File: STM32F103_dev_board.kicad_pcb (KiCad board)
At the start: 4 copper layers, 39.4 x 83.8 mm, 37 parts, among them IC1 TLV70233DBVR, IC2 FT232RNL-REEL, J1 Conn_ARM_JTAG_SWD_20, J2 Conn_01x20_Pin, J3 Conn_01x20_Pin, J4 Conn_02x03_Odd_Even, J6 USB4800-03-A, U1 STM32F103RBTx, Y1 8MHz, Y2 Crystal_GND23

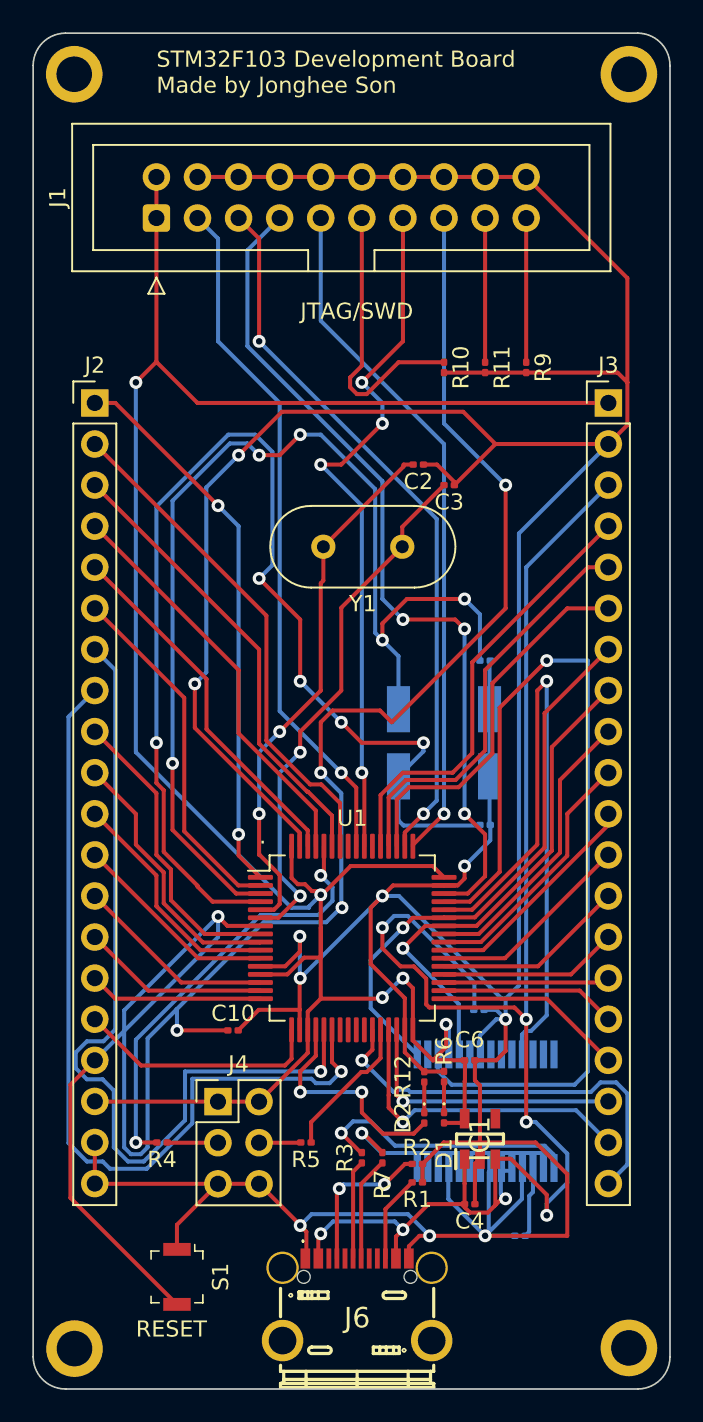
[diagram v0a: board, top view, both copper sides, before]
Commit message: Changed 0603 footprints to hand solderable ones
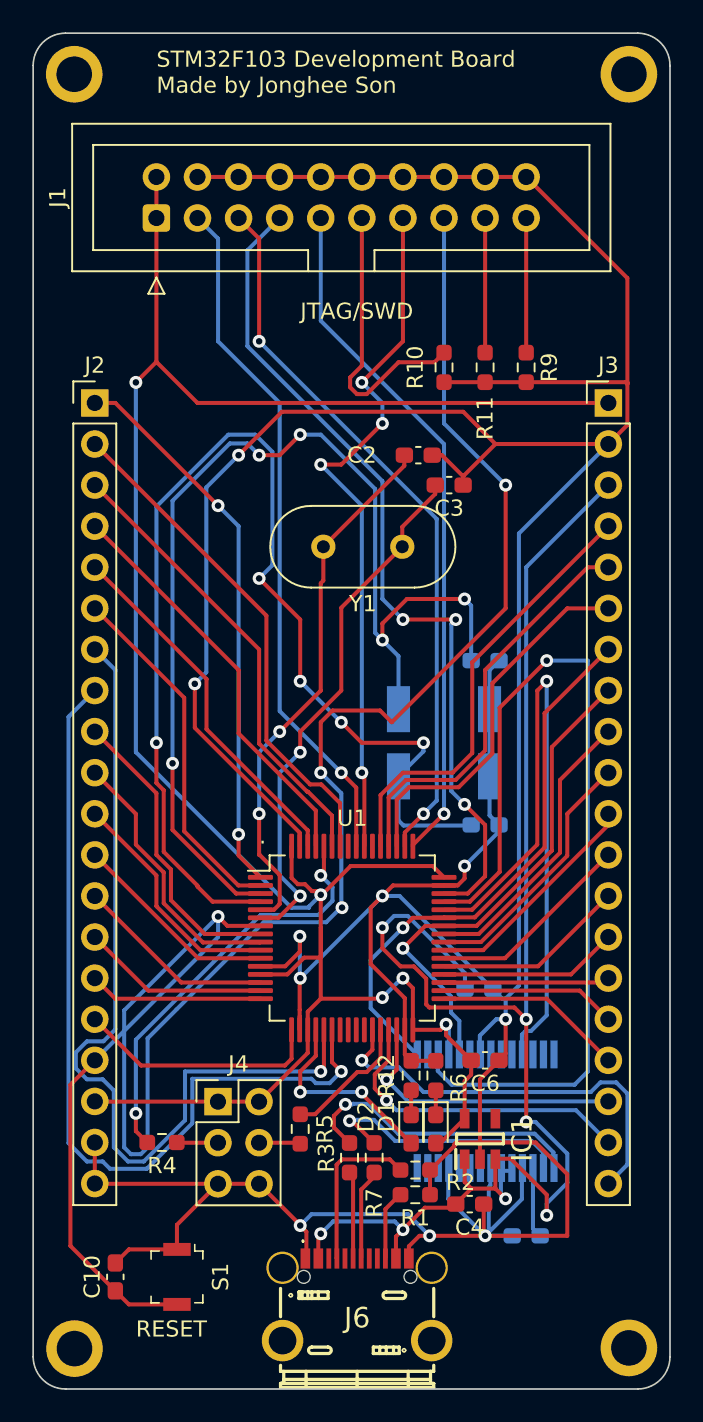
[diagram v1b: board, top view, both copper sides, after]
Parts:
- C1, C10, C11, C12, C2, C3, C4, C5, C6: footprint Capacitor_SMD:C_0201_0603Metric -> Capacitor_SMD:C_0603_1608Metric_Pad1.08x0.95mm_HandSolder
- D1, D2: footprint LED_SMD:LED_0201_0603Metric -> LED_SMD:LED_0603_1608Metric_Pad1.05x0.95mm_HandSolder
- R1, R10, R11, R12, R2, R3, R4, R5, R6, R7, R9: footprint Resistor_SMD:R_0201_0603Metric -> Resistor_SMD:R_0603_1608Metric_Pad0.98x0.95mm_HandSolder
- moved C10 16.9 mm to (130.8, 134.6), turned to 90 degrees
- moved C1 1.27 mm to (153.3, 116.8)
- moved D2 1.06 mm to (149.1, 125.5)
- moved C6 0.95 mm to (153.7, 121.2)
- moved R5 0.91 mm to (142.2, 125.5), turned to -90 degrees
- moved D1 0.86 mm to (150.6, 125.5)
- moved R12 0.81 mm to (149.1, 122.2)
- moved R1 0.77 mm to (149.4, 129.5)
- moved R3 0.76 mm to (145.3, 127.3)
- moved C2 0.58 mm to (149.5, 83.8)
- moved R6 0.51 mm to (150.6, 122.2)
- moved R7 0.51 mm to (146.8, 127.3)
- moved R2 0.40 mm to (149.4, 128.0)
- moved C5 0.38 mm to (156.2, 132.1)
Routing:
- net /5V: track 101.8 -> 98.7 mm
- net /GND: track 307.3 -> 304.3 mm
- net /RESET: track 278.4 -> 275.7 mm, vias 10 -> 9
- net /PA4: track 14.0 -> 12.5 mm
- net /USBDM: track 14.5 -> 15.9 mm
- net /USBDP: track 17.0 -> 18.3 mm
- net Net-(J6-CC2): track 5.39 -> 4.35 mm
- net /BOOT0: track 27.1 -> 26.1 mm
- net Net-(J6-DN1): track 6.50 -> 5.65 mm
- net /BOOT1: track 8.94 -> 8.15 mm
- net Net-(J6-DP1): track 6.13 -> 5.41 mm
- net Net-(J6-CC1): track 9.52 -> 10.2 mm, vias 2 -> 0
- net Net-(J4-Pin_3): track 3.15 -> 2.55 mm
- net Net-(J1-DBGRQ/NC): track 8.92 -> 8.32 mm
- net Net-(J1-DBGACK/NC): track 8.92 -> 8.32 mm
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
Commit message: Fixed some labels and updated production files
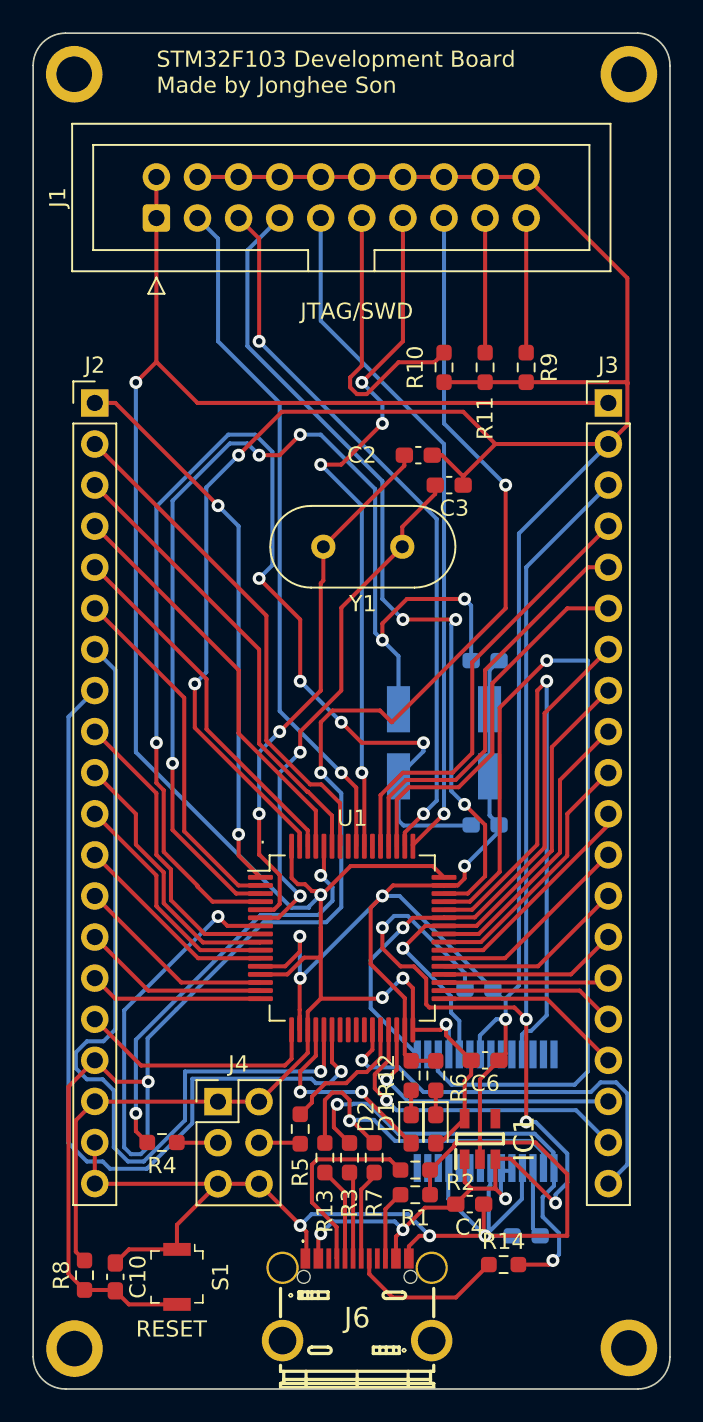
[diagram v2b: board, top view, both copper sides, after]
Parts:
- added R13: 20, Resistor_SMD:R_0603_1608Metric_Pad0.98x0.95mm_HandSolder, F.Cu at (143.8, 127.3)
- added R14: 20, Resistor_SMD:R_0603_1608Metric_Pad0.98x0.95mm_HandSolder, F.Cu at (154.8, 133.9)
- added R8: 0, Resistor_SMD:R_0603_1608Metric_Pad0.98x0.95mm_HandSolder, F.Cu at (128.9, 134.5)
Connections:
- net /5V renamed 5V
- net /GND renamed GND
- net /PA10/USART1_RX renamed PA10/USART1_RX
- net /PA9/USART1_TX renamed PA9/USART1_TX
- net /USBDM renamed USBDM
- net /USBDP renamed USBDP
- net /VBAT renamed VBAT
- C10 pad 1: /RESET -> RESET
- C6 pad 2: /RESET -> VCC3V3
- D1 pad 2: /RESET -> VCC3V3
- IC1 pad 5: /RESET -> VCC3V3
- IC2 pad 4: /RESET -> VCC3V3
- J1 pad 1: /RESET -> VCC3V3
- J1 pad 15: /RESET -> RESET
- J1 pad 2: /RESET -> VCC3V3
- J2 pad 17: /RESET -> RESET
- J2 pad 18: /RESET -> VCC3V3
- J3 pad 1: /RESET -> VCC3V3
- J4 pad 1: /RESET -> VCC3V3
- J4 pad 2: /RESET -> VCC3V3
- J6 pad B6: unconnected-(J6-DP2-PadB6) -> Net-(J6-DP2)
- J6 pad B7: unconnected-(J6-DN2-PadB7) -> Net-(J6-DN2)
- S1 pad 2: /RESET -> RESET
- U1 pad 13: /RESET -> VCC3V3
- U1 pad 19: /RESET -> VCC3V3
- U1 pad 32: /RESET -> VCC3V3
- U1 pad 48: /RESET -> VCC3V3
- U1 pad 64: /RESET -> VCC3V3
- U1 pad 7: /RESET -> RESET
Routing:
- net /RESET: track 275.7 -> 0.00 mm, vias 9 -> 0
- net VCC3V3: track 0.00 -> 157.9 mm, vias 0 -> 5
- net RESET: track 0.00 -> 121.2 mm, vias 0 -> 4
- net Net-(J6-DP2): track 0.00 -> 9.79 mm
- net USBDP: track 18.3 -> 27.4 mm, vias 1 -> 2
- net USBDM: track 15.9 -> 21.7 mm
- net Net-(J6-DN2): track 0.00 -> 5.83 mm
- net Net-(J6-CC1): track 10.2 -> 12.3 mm
- net 5V: track 98.7 -> 97.2 mm
- added copper zone on In1.Cu, net VCC3V3
- removed copper zone on In1.Cu, net /RESET

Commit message: Removed external pull-up resistor in reset switch
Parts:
- removed R8: 0, Resistor_SMD:R_0603_1608Metric_Pad0.98x0.95mm_HandSolder
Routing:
- net VCC3V3: track 157.9 -> 147.4 mm
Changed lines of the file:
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@@
     (title "STM32F103RBT6 Dev Board")
     (date "2023-10-13")
-    (rev "1.1.1")
+    (rev "1.1.2")
   )
   (layers
@@
     )
   )
-  (footprint "Resistor_SMD:R_0603_1608Metric_Pad0.98x0.95mm_HandSolder" (layer "F.Cu")
-    (at 128.905 134.5165 90)
-    (descr "Resistor SMD 0603 (1608 Metric), square (rectangular) end terminal, IPC_7351 nominal with elongated pad for handsoldering. (Body size source: IPC-SM-782 page 72, https://www.pcb-3d.com/wordpress/wp-content/uploads/ipc-sm-782a_amendment_1_and_2.pdf), generated with kicad-footprint-generator")
-    (tags "resistor handsolder")
-    (property "Sheetfile" "STM32F103_dev_board.kicad_sch")
-    (property "Sheetname" "")
-    (property "ki_description" "Resistor")
-    (property "ki_keywords" "R res resistor")
-    (attr smd)
-    (fp_text reference "R8" (at 0 -1.43 90) (layer "F.SilkS")
-        (effects (font (size 1 1) (thickness 0.15)))
-    )
-    (fp_text value "0" (at 0 1.43 90) (layer "F.Fab")
-        (effects (font (size 1 1) (thickness 0.15)))
-    )
-    (fp_text user "${REFERENCE}" (at 0 0 90) (layer "F.Fab")
-        (effects (font (size 0.4 0.4) (thickness 0.06)))
-    )
-    (fp_line (start -0.254724 -0.5225) (end 0.254724 -0.5225)
-      (stroke (width 0.12) (type solid)) (layer "F.SilkS"))
-    (fp_line (start -0.254724 0.5225) (end 0.254724 0.5225)
-      (stroke (width 0.12) (type solid)) (layer "F.SilkS"))
-    (fp_line (start -1.65 -0.73) (end 1.65 -0.73)
-      (stroke (width 0.05) (type solid)) (layer "F.CrtYd"))
-    (fp_line (start -1.65 0.73) (end -1.65 -0.73)
-      (stroke (width 0.05) (type solid)) (layer "F.CrtYd"))
-    (fp_line (start 1.65 -0.73) (end 1.65 0.73)
-      (stroke (width 0.05) (type solid)) (layer "F.CrtYd"))
-    (fp_line (start 1.65 0.73) (end -1.65 0.73)
-      (stroke (width 0.05) (type solid)) (layer "F.CrtYd"))
-    (fp_line (start -0.8 -0.4125) (end 0.8 -0.4125)
-      (stroke (width 0.1) (type solid)) (layer "F.Fab"))
-    (fp_line (start -0.8 0.4125) (end -0.8 -0.4125)
-      (stroke (width 0.1) (type solid)) (layer "F.Fab"))
-    (fp_line (start 0.8 -0.4125) (end 0.8 0.4125)
-      (stroke (width 0.1) (type solid)) (layer "F.Fab"))
-    (fp_line (start 0.8 0.4125) (end -0.8 0.4125)
-      (stroke (width 0.1) (type solid)) (layer "F.Fab"))
-    (pad "1" smd roundrect (at -0.9125 0 90) (size 0.975 0.95) (layers "F.Cu" "F.Paste" "F.Mask") (roundrect_rratio 0.25)
-      (net 80 "RESET") (pintype "passive"))
-    (pad "2" smd roundrect (at 0.9125 0 90) (size 0.975 0.95) (layers "F.Cu" "F.Paste" "F.Mask") (roundrect_rratio 0.25)
-      (net 83 "VCC3V3") (pintype "passive"))
-    (model "${KICAD6_3DMODEL_DIR}/Resistor_SMD.3dshapes/R_0603_1608Metric.wrl"
-      (offset (xyz 0 0 0))
-      (scale (xyz 1 1 1))
-      (rotate (xyz 0 0 0))
-    )
-  )
   (footprint "Package_QFP:LQFP-64_10x10mm_P0.5mm" (layer "F.Cu")
     (at 145.455 113.67)
@@
     (pad "28" smd rect (at 3.512 4.225 180) (size 0.45 1.725) (layers "B.Cu" "B.Paste" "B.Mask")
       (net 79 "unconnected-(IC2-OSCO-Pad28)") (pinfunction "OSCO") (pintype "passive"))
-    (model "C:\\lib\\KiCad_Library\\SamacSys_Parts.3dshapes\\FT232RNL-REEL.stp"
+    (model "C:\\lib\\samacsys\\SamacSys_Parts.3dshapes\\FT232RNL-REEL.stp"
       (offset (xyz 0 0 0))
       (scale (xyz 1 1 1))
@@
   (segment (start 158.75 128.805) (end 158.75 127) (width 0.25) (layer "B.Cu") (net 82))
   (segment (start 148.045 112.305) (end 147.32 113.03) (width 0.25) (layer "B.Cu") (net 82))
-  (segment (start 128.905 133.604) (end 128.365 133.064) (width 0.25) (layer "F.Cu") (net 83))
   (segment (start 152.8075 122.1175) (end 152.405 122.52) (width 0.25) (layer "F.Cu") (net 83))
   (segment (start 151.257 119.6795) (end 151.257 118.999) (width 0.25) (layer "F.Cu") (net 83))
@@
   (segment (start 135.89 80.59) (end 133.35 78.05) (width 0.25) (layer "F.Cu") (net 83))
   (segment (start 141.444695 115.92) (end 139.78 115.92) (width 0.25) (layer "F.Cu") (net 83))
-  (segment (start 128.365 124.945) (end 129.54 123.77) (width 0.25) (layer "F.Cu") (net 83))
   (segment (start 142.540305 110.345) (end 142.965 110.769695) (width 0.25) (layer "F.Cu") (net 83))
   (segment (start 152.8075 121.23) (end 151.257 119.6795) (width 0.25) (layer "F.Cu") (net 83))
@@
   (segment (start 149.205 119.345) (end 149.205 116.765) (width 0.25) (layer "F.Cu") (net 83))
   (segment (start 143.51 113.030685) (end 143.51 114.88) (width 0.25) (layer "F.Cu") (net 83))
-  (segment (start 128.365 133.064) (end 128.365 124.945) (width 0.25) (layer "F.Cu") (net 83))
   (segment (start 142.484695 114.88) (end 141.444695 115.92) (width 0.25) (layer "F.Cu") (net 83))
   (segment (start 152.34 125.1) (end 152.4 125.04) (width 0.25) (layer "F.Cu") (net 83))

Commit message: Changed net labels into global labels
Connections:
- net /BOOT0 renamed BOOT0
- net /BOOT1 renamed BOOT1
- net /JNTRST renamed JNTRST
- net /JTCK/SWCLK renamed JTCK/SWCLK
- net /JTDI renamed JTDI
- net /JTDO renamed JTDO
- net /JTMS/SWDIO renamed JTMS/SWDIO
- net /OSC32_IN renamed OSC32_IN
- net /OSC32_OUT renamed OSC32_OUT
- net /OSC_IN renamed OSC_IN
- net /OSC_OUT renamed OSC_OUT
- net /PA0 renamed PA0
- net /PA1 renamed PA1
- net /PA11 renamed PA11
- net /PA12 renamed PA12
- net /PA2 renamed PA2
- net /PA3 renamed PA3
- net /PA4 renamed PA4
- net /PA5 renamed PA5
- net /PA6 renamed PA6
- net /PA7 renamed PA7
- net /PA8 renamed PA8
- net /PB0 renamed PB0
- net /PB1 renamed PB1
- net /PB10 renamed PB10
- net /PB11 renamed PB11
- net /PB12 renamed PB12
- net /PB13 renamed PB13
- net /PB14 renamed PB14
- net /PB15 renamed PB15
- net /PB5 renamed PB5
- net /PB6 renamed PB6
- net /PB7 renamed PB7
- net /PB8 renamed PB8
- net /PB9 renamed PB9
- net /PC0 renamed PC0
- net /PC1 renamed PC1
- net /PC10 renamed PC10
- net /PC11 renamed PC11
- net /PC12 renamed PC12
- net /PC13 renamed PC13
- net /PC2 renamed PC2
- net /PC3 renamed PC3
- net /PC4 renamed PC4
- net /PC5 renamed PC5
- net /PC6 renamed PC6
- net /PC7 renamed PC7
- net /PC8 renamed PC8
- net /PC9 renamed PC9
